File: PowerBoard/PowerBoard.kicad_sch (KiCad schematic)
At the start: 7 parts, among them J1 PowerOut, P1 USB_C_Receptacle_USB2.0_14P, U1 MCP73811T-420I-OT

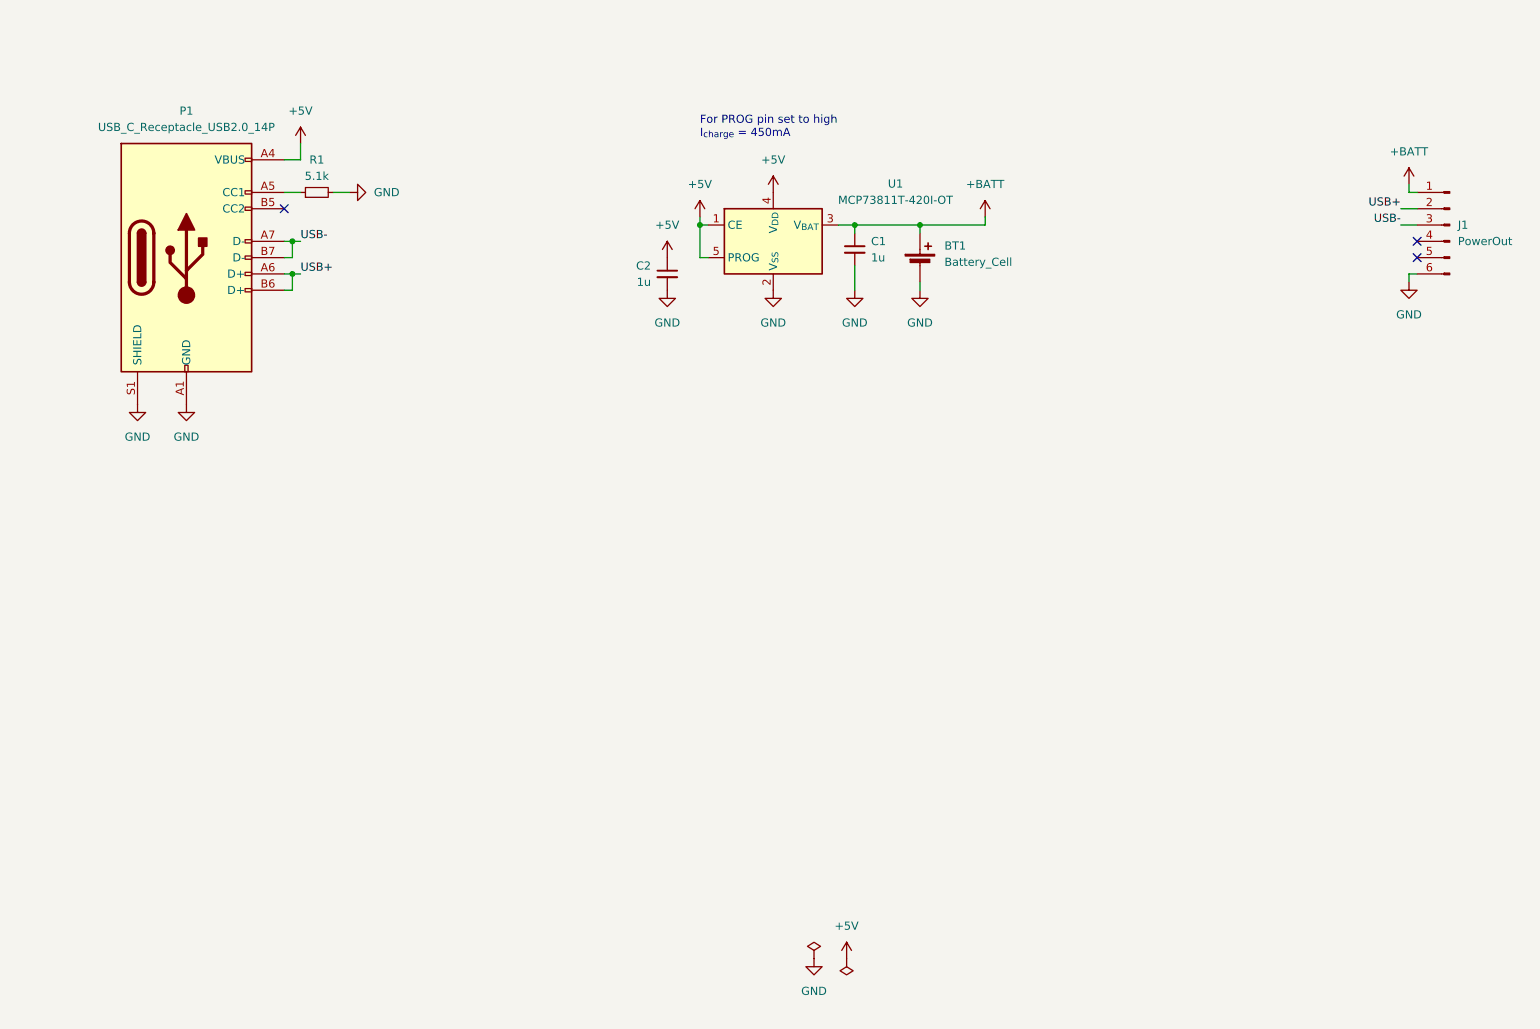
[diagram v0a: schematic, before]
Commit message: change schematic, use touch controller to enable second bard power. microcontroller should set pin up to latch power
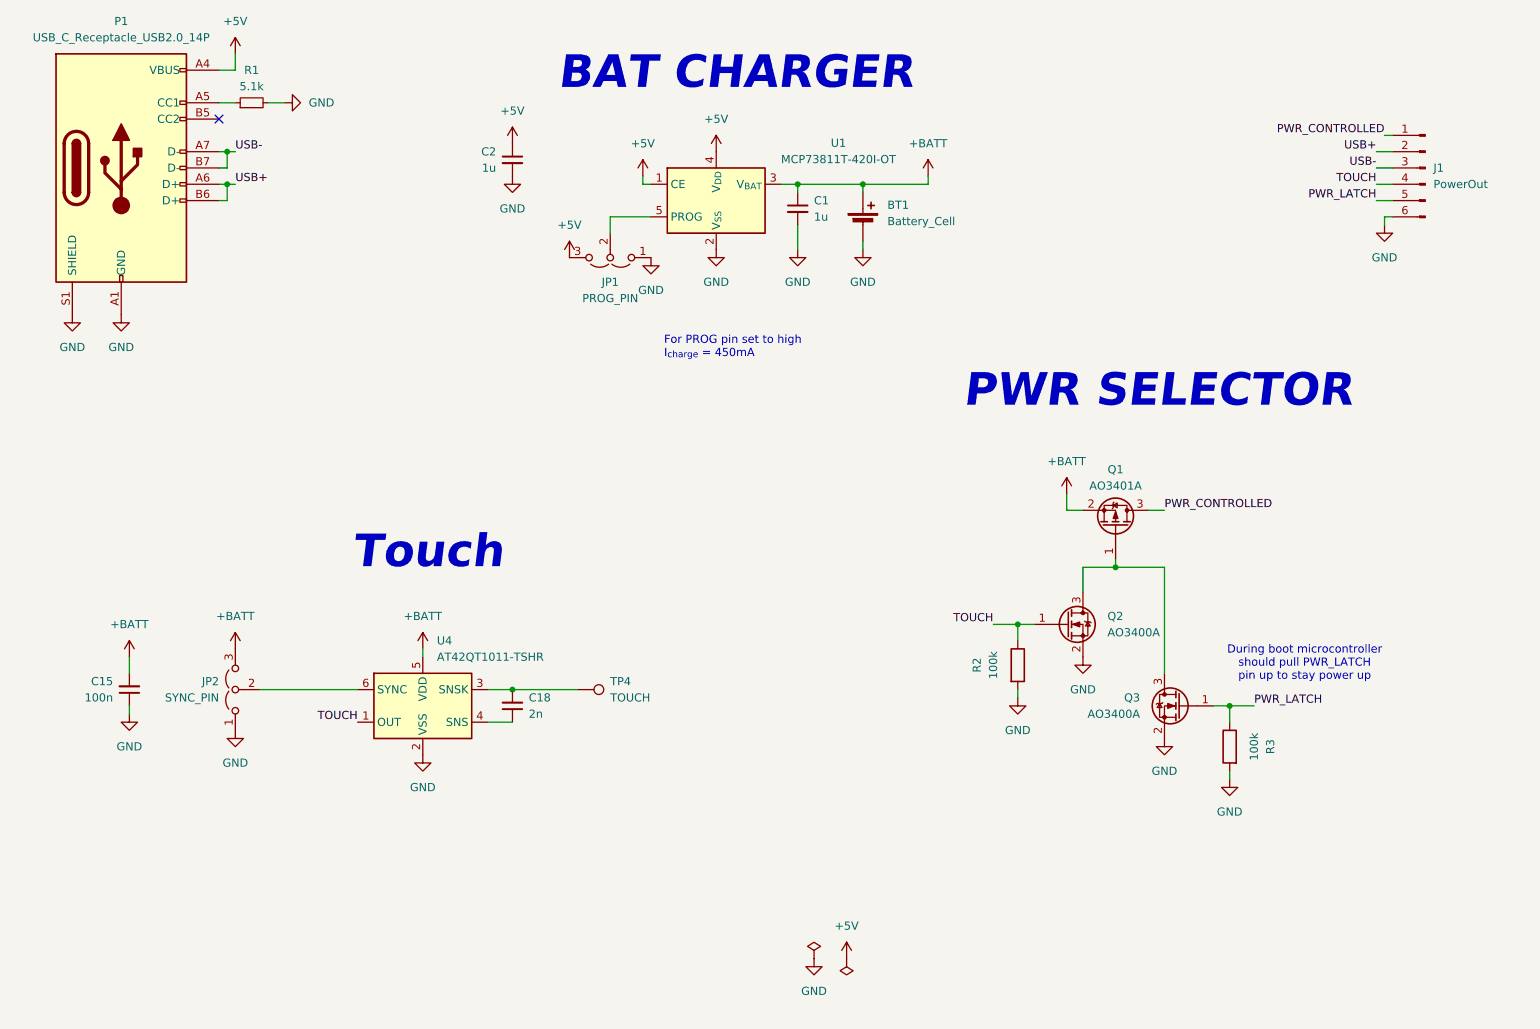
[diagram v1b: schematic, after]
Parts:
- added C15: 100n, Capacitor_SMD:C_0603_1608Metric_Pad1.08x0.95mm_HandSolder, symbol Device:C_Small
- added C18: 2n, Capacitor_SMD:C_0603_1608Metric_Pad1.08x0.95mm_HandSolder, symbol Device:C_Small
- added JP1: PROG_PIN, symbol Jumper:Jumper_3_Open
- added JP2: SYNC_PIN, symbol Jumper:Jumper_3_Open
- added Q1: AO3401A, Package_TO_SOT_SMD:SOT-23, symbol Transistor_FET:AO3401A
- added Q2, Q3: AO3400A, Package_TO_SOT_SMD:SOT-23, symbol Transistor_FET:AO3400A
- added R2, R3: 100k, Resistor_SMD:R_0603_1608Metric_Pad0.98x0.95mm_HandSolder, symbol Device:R
- added TP4: TOUCH, TestPoint:TestPoint_Pad_D3.0mm, symbol Connector:TestPoint
- added U4: AT42QT1011-TSHR, Package_TO_SOT_SMD:SOT-23-6, symbol Sensor_Touch:AT42QT1011-TSHR
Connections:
- net +5V: now also JP1.3 (B); no longer U1.5 (PROG)
- net +BATT: now also C15.2, JP2.3 (B), Q1.2 (S), U4.5 (VDD); no longer J1.1 (Pin_1)
- net GND: now also C15.1, JP1.1 (A), JP2.1 (A), Q2.2 (S), Q3.2 (S), R2.2, R3.2, U4.2 (VSS)
- net TOUCH: now reaches J1.4 (Pin_4)
- net TOUCH: now also Q2.1 (G), R2.1, U4.1 (OUT)
- net PWR_LATCH: now reaches J1.5 (Pin_5)
- net PWR_LATCH: now also Q3.1 (G), R3.1
- new net: Q1.1 (G), Q2.3 (D), Q3.3 (D)
- new net: JP1.2 (C), U1.5 (PROG)
- new net: C18.2, TP4.1, U4.3 (SNSK)
- new net: C18.1, U4.4 (SNS)
- new net: JP2.2 (C), U4.6 (SYNC)
- new net PWR_CONTROLLED: J1.1 (Pin_1), Q1.3 (D)
- no-connect marks 3 -> 1
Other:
- note added: "BAT CHARGER"
- note added: "During boot microcontroller should pull PWR_LATCH pin up to stay power up"
- note added: "PWR SELECTOR"
- note added: "Touch"
- moved on the sheet: BT1, C1, C2, J1, P1, R1, U1

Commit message: Change location of tuch sensor, touch button now power up all components, change length. Add buzzer to mainboard and remove touch from them. change revision version
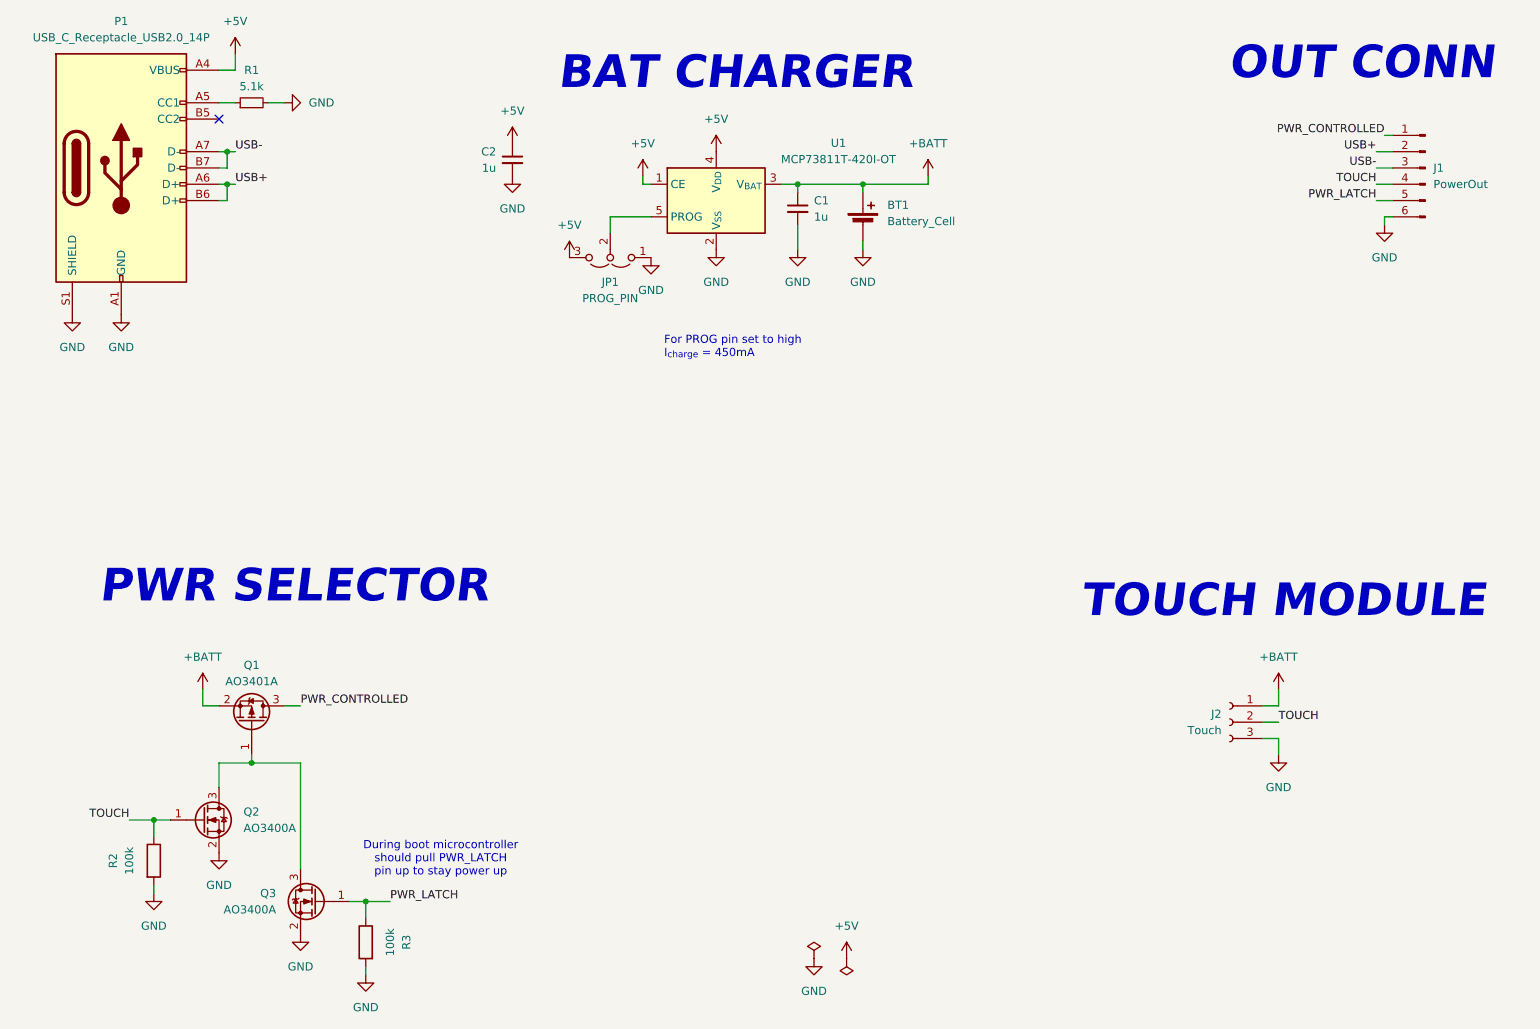
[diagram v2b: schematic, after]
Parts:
- removed C15: 100n, Capacitor_SMD:C_0603_1608Metric_Pad1.08x0.95mm_HandSolder, symbol Device:C_Small
- removed C18: 2n, Capacitor_SMD:C_0603_1608Metric_Pad1.08x0.95mm_HandSolder, symbol Device:C_Small
- removed JP2: SYNC_PIN, symbol Jumper:Jumper_3_Open
- removed TP4: TOUCH, TestPoint:TestPoint_Pad_D3.0mm, symbol Connector:TestPoint
- removed U4: AT42QT1011-TSHR, Package_TO_SOT_SMD:SOT-23-6, symbol Sensor_Touch:AT42QT1011-TSHR
- added J2: Touch, Connector_Molex:Molex_PicoBlade_53047-0310_1x03_P1.25mm_Vertical, symbol Connector:Conn_01x03_Socket
- JP1: footprint (none) -> Jumper:SolderJumper-3_P1.3mm_Open_RoundedPad1.0x1.5mm
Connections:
- net +BATT: now also J2.1 (Pin_1)
- net GND: now also J2.3 (Pin_3)
- net TOUCH: now also J2.2 (Pin_2)
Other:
- note added: "OUT CONN"
- note added: "TOUCH MODULE"
- note removed: "Touch"
- company: (none) -> Miłosz Derżko
- title: (none) -> blob
- moved on the sheet: Q1, Q2, Q3, R2, R3
